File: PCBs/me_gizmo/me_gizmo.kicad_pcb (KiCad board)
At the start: 4 copper layers, 89.4 x 49.5 mm, 136 parts, among them J1 PushButton_Terminal_01x06, J2 PushButton_Terminal_01x06, J3 PushButton_Terminal_01x06, J4 PushButton_Terminal_01x06, J5 Debug, J6 USB4105-GF-A, Q1 MMBT3904L, U1 ADG714, U10 RP2350A, U11 MCP4922, U12 MCP4922, U13 MCP1702T-3302E_CB, U2 ADG714, U3 ADG714, U4 ADG714, U5 REF35250QDBVR, U6 TMP126-Q1, U7 ADG714, U8 TLV9151, U9 MCP3564R, X1 IQXO-791, X4 SG-8018CG_19.6608M-TJHSA3

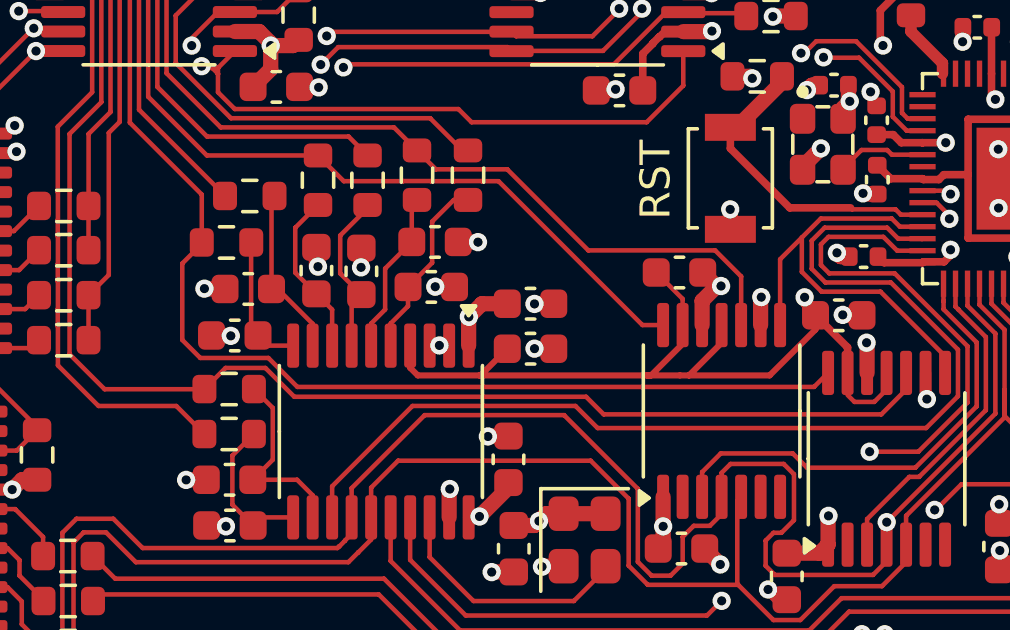
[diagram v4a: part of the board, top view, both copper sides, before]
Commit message: Switched the DAC connections on channels 3 and 4 to reflect the flipped bridge configurations
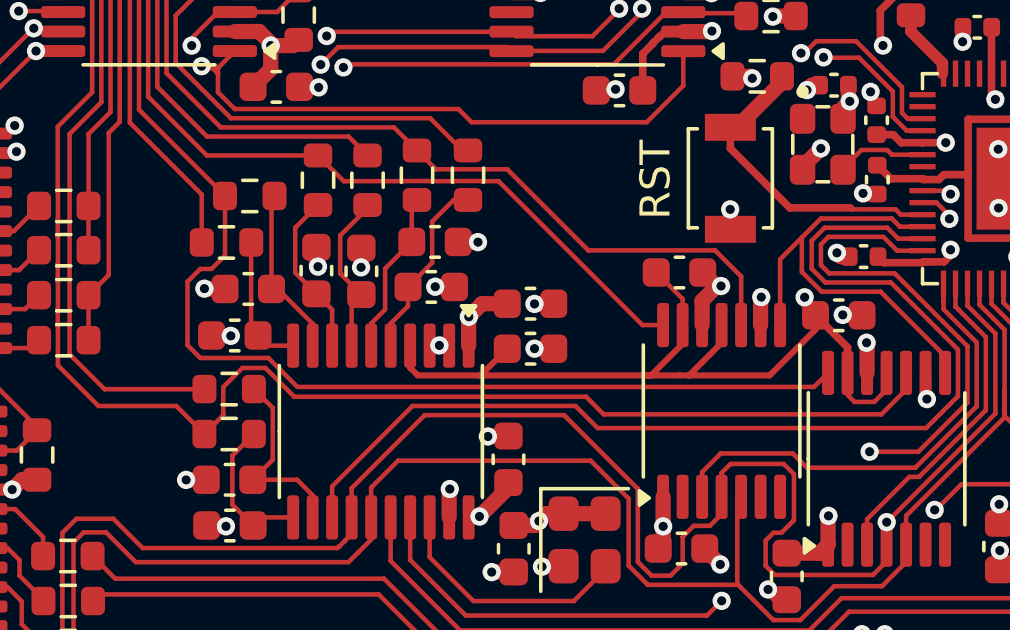
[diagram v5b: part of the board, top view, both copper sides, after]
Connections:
- U12 pad 10: /ADC/DAC/CH4/ADC4- -> /ADC/DAC/CH4/ADC4+
- U12 pad 14: /ADC/DAC/CH3/ADC3- -> /ADC/DAC/CH3/ADC3+
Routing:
- net /ADC/DAC/CH3/ADC3+: track 27.2 -> 55.0 mm
- net /ADC/DAC/CH4/ADC4+: track 48.9 -> 75.3 mm
- net /ADC/DAC/CH3/ADC3-: track 56.2 -> 30.3 mm
- net /ADC/DAC/CH4/ADC4-: track 68.8 -> 43.6 mm
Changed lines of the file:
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@@
 			(layers "F.Cu" "F.Mask" "F.Paste")
 			(roundrect_rratio 0.25)
-			(net 33 "/ADC/DAC/CH4/ADC4-")
+			(net 31 "/ADC/DAC/CH4/ADC4+")
 			(pinfunction "VOUTB")
 			(pintype "output")
@@
 			(layers "F.Cu" "F.Mask" "F.Paste")
 			(roundrect_rratio 0.25)
-			(net 26 "/ADC/DAC/CH3/ADC3-")
+			(net 28 "/ADC/DAC/CH3/ADC3+")
 			(pinfunction "VOUTA")
 			(pintype "output")
@@
 	)
 	(segment
-		(start 198.9598 94.1832)
-		(end 199.427 93.716)
-		(width 0.1524)
-		(layer "F.Cu")
-		(net 26)
-	)
-	(segment
-		(start 181.736954 94.1832)
-		(end 198.9598 94.1832)
-		(width 0.1524)
-		(layer "F.Cu")
-		(net 26)
-	)
-	(segment
-		(start 177.9004 90.067)
-		(end 177.9004 92.617336)
-		(width 0.1524)
-		(layer "F.Cu")
-		(net 26)
-	)
-	(segment
-		(start 180.771354 93.2176)
-		(end 181.736954 94.1832)
-		(width 0.1524)
-		(layer "F.Cu")
-		(net 26)
-	)
-	(segment
 		(start 176.4284 78.486)
 		(end 176.4284 79.026198)
@@
 	)
 	(segment
-		(start 178.5498 89.4176)
-		(end 177.9004 90.067)
-		(width 0.1524)
-		(layer "F.Cu")
-		(net 26)
-	)
-	(segment
 		(start 174.784049 77.7864)
 		(end 174.859655 77.710794)
@@
 	)
 	(segment
-		(start 177.9004 92.617336)
-		(end 178.500664 93.2176)
-		(width 0.1524)
-		(layer "F.Cu")
-		(net 26)
-	)
-	(segment
 		(start 173.9292 77.7864)
 		(end 174.784049 77.7864)
@@
 	)
 	(segment
-		(start 178.500664 93.2176)
-		(end 180.771354 93.2176)
-		(width 0.1524)
-		(layer "F.Cu")
-		(net 26)
-	)
-	(segment
 		(start 176.151965 79.302633)
 		(end 176.151965 85.372365)
@@
 	)
 	(segment
+		(start 180.771354 93.2176)
+		(end 178.500664 93.2176)
+		(width 0.1524)
+		(layer "F.Cu")
+		(net 28)
+	)
+	(segment
+		(start 181.736954 94.1832)
+		(end 180.771354 93.2176)
+		(width 0.1524)
+		(layer "F.Cu")
+		(net 28)
+	)
+	(segment
 		(start 179.3248 87.8086)
 		(end 176.457766 84.941566)
@@
 	)
 	(segment
+		(start 179.3248 89.8002)
+		(end 179.3248 87.8176)
+		(width 0.1524)
+		(layer "F.Cu")
+		(net 28)
+	)
+	(segment
+		(start 178.075 90.675)
+		(end 178.5 90.25)
+		(width 0.1524)
+		(layer "F.Cu")
+		(net 28)
+	)
+	(segment
 		(start 174.8963 76.075696)
 		(end 174.8963 70.7817)
@@
 	)
 	(segment
+		(start 178.075 92.791936)
+		(end 178.075 90.675)
+		(width 0.1524)
+		(layer "F.Cu")
+		(net 28)
+	)
+	(segment
+		(start 198.9598 94.1832)
+		(end 181.736954 94.1832)
+		(width 0.1524)
+		(layer "F.Cu")
+		(net 28)
+	)
+	(segment
+		(start 199.427 93.716)
+		(end 198.9598 94.1832)
+		(width 0.1524)
+		(layer "F.Cu")
+		(net 28)
+	)
+	(segment
+		(start 178.5 90.25)
+		(end 178.875 90.25)
+		(width 0.1524)
+		(layer "F.Cu")
+		(net 28)
+	)
+	(segment
 		(start 174.8963 70.7817)
 		(end 174.0916 69.977)
@@
 	)
 	(segment
+		(start 178.500664 93.2176)
+		(end 178.075 92.791936)
+		(width 0.1524)
+		(layer "F.Cu")
+		(net 28)
+	)
+	(segment
+		(start 178.875 90.25)
+		(end 179.3248 89.8002)
+		(width 0.1524)
+		(layer "F.Cu")
+		(net 28)
+	)
+	(segment
 		(start 174.09 69.95)
 		(end 174.09 64.95)
@@
 	)
 	(segment
+		(start 201.201796 95.0976)
+		(end 191.9478 95.0976)
+		(width 0.1524)
+		(layer "F.Cu")
+		(net 31)
+	)
+	(segment
 		(start 173.75 88.613088)
 		(end 173.75 89.161912)
@@
 	)
 	(segment
+		(start 179.2676 94.187112)
+		(end 179.2676 95.1228)
+		(width 0.1524)
+		(layer "F.Cu")
+		(net 31)
+	)
+	(segment
 		(start 173.9292 80.3864)
 		(end 174.4864 80.3864)
@@
 	)
 	(segment
+		(start 179.2676 95.1228)
+		(end 178.637 95.7534)
+		(width 0.1524)
+		(layer "F.Cu")
+		(net 31)
+	)
+	(segment
 		(start 174.8963 84.3615)
 		(end 173.75 85.5078)
@@
 	)
 	(segment
+		(start 202.027 94.272396)
+		(end 201.201796 95.0976)
+		(width 0.1524)
+		(layer "F.Cu")
+		(net 31)
+	)
+	(segment
 		(start 173.7546 89.166512)
 		(end 173.7546 90.083488)
@@
 	)
 	(segment
+		(start 202.027 93.716)
+		(end 202.027 94.272396)
+		(width 0.1524)
+		(layer "F.Cu")
+		(net 31)
+	)
+	(segment
 		(start 173.7546 88.608488)
 		(end 173.75 88.613088)
@@
 	)
 	(segment
+		(start 191.9478 95.0976)
+		(end 191.3616 94.5114)
+		(width 0.1524)
+		(layer "F.Cu")
+		(net 31)
+	)
+	(segment
 		(start 173.75 87.686912)
 		(end 173.7546 87.691512)
@@
 	)
 	(segment
+		(start 180.671488 93.5502)
+		(end 179.904512 93.5502)
+		(width 0.1524)
+		(layer "F.Cu")
+		(net 31)
+	)
+	(segment
 		(start 173.7546 92.166512)
 		(end 173.7546 93.4652)
@@
 	)
 	(segment
+		(start 179.904512 93.5502)
+		(end 179.2676 94.187112)
+		(width 0.1524)
+		(layer "F.Cu")
+		(net 31)
+	)
+	(segment
+		(start 181.632688 94.5114)
+		(end 180.671488 93.5502)
+		(width 0.1524)
+		(layer "F.Cu")
+		(net 31)
+	)
+	(segment
 		(start 177.7018 94.8182)
 		(end 178.637 95.7534)
@@
 		(net 31)
 	)
+	(segment
+		(start 191.3616 94.5114)
+		(end 181.632688 94.5114)
+		(width 0.1524)
+		(layer "F.Cu")
+		(net 31)
+	)
 	(via
 		(at 159.131 74.0918)
@@
 	)
 	(segment
-		(start 201.201796 95.0976)
-		(end 191.9478 95.0976)
-		(width 0.1524)
-		(layer "F.Cu")
-		(net 33)
-	)
-	(segment
 		(start 175.2021 79.802904)
 		(end 174.485596 79.0864)
@@
 	)
 	(segment
-		(start 180.671488 93.5502)
-		(end 179.3426 93.5502)
-		(width 0.1524)
-		(layer "F.Cu")
-		(net 33)
-	)
-	(segment
 		(start 173.372804 79.0864)
 		(end 173.126404 78.84)
@@
 	)
 	(segment
-		(start 202.027 94.272396)
-		(end 201.201796 95.0976)
-		(width 0.1524)
-		(layer "F.Cu")
-		(net 33)
-	)
-	(segment
 		(start 173.049804 78.7634)
 		(end 170.3705 78.7634)
@@
 	)
 	(segment
-		(start 202.027 93.716)
-		(end 202.027 94.272396)
-		(width 0.1524)
-		(layer "F.Cu")
-		(net 33)
-	)
-	(segment
 		(start 175.3108 94.2594)
 		(end 174.1424 93.091)
@@
 	)
 	(segment
-		(start 179.3426 93.5502)
-		(end 178.638 94.2548)
-		(width 0.1524)
-		(layer "F.Cu")
-		(net 33)
-	)
-	(segment
 		(start 173.9292 79.0864)
 		(end 173.372804 79.0864)
@@
 	)
 	(segment
-		(start 191.9478 95.0976)
-		(end 191.3616 94.5114)
-		(width 0.1524)
-		(layer "F.Cu")
-		(net 33)
-	)
-	(segment
 		(start 174.1424 93.091)
 		(end 174.1424 85.7504)
@@
 	)
 	(segment
-		(start 181.632688 94.5114)
-		(end 180.671488 93.5502)
-		(width 0.1524)
-		(layer "F.Cu")
-		(net 33)
-	)
-	(segment
 		(start 178.6334 94.2594)
 		(end 175.3108 94.2594)
 		(width 0.1524)
 		(layer "F.Cu")
-		(net 33)
-	)
-	(segment
-		(start 191.3616 94.5114)
-		(end 181.632688 94.5114)
-		(width 0.1524)
-		(layer "F.Cu")

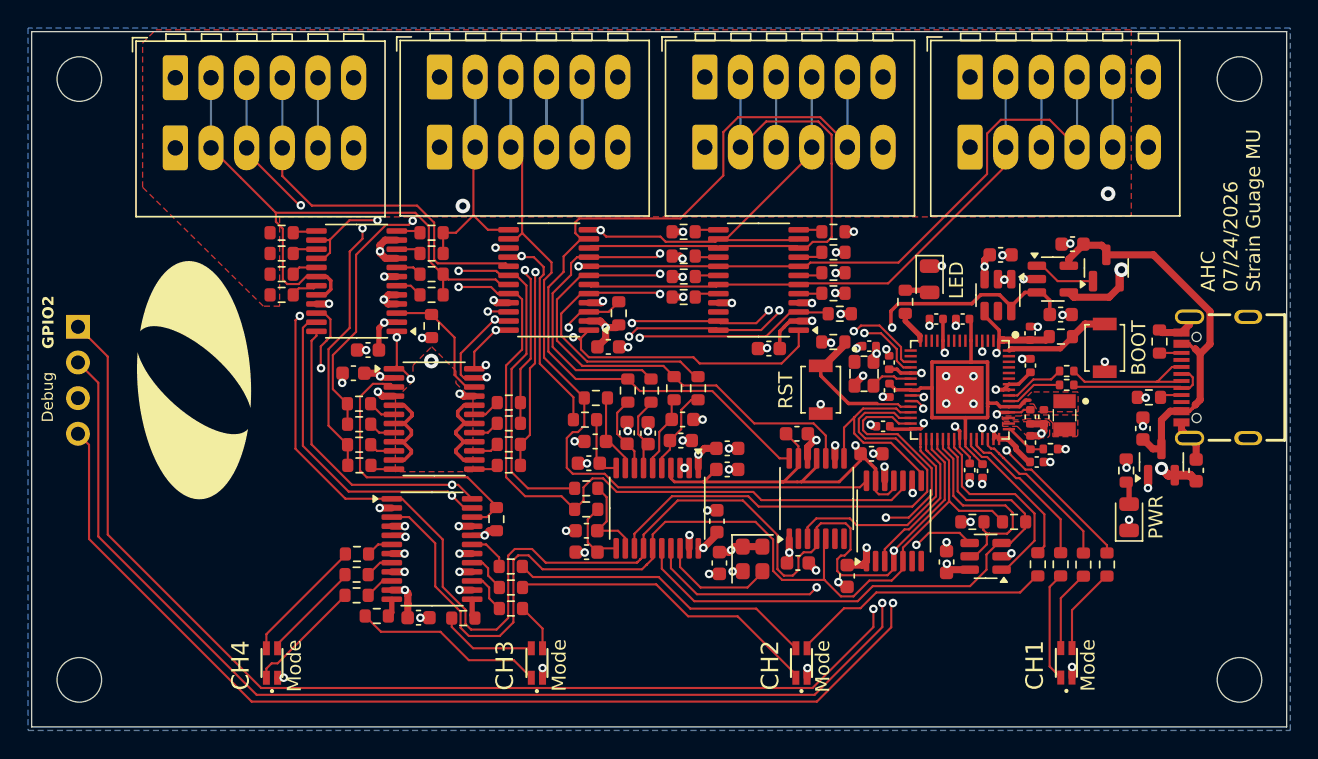
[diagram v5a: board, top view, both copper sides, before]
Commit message: Added Main.py with a channel configuration detection script. Also added a thread that updates the leds to display what the device thinks the current operating mode is, particularly while actively looping detect_config. Finally, there are a bunch of untested updates (mostly software) to make the code compatible with the new board. Any replaced working protoype code exists underneath the revisions labeled with 'protptype above it. This commit contains a few key revisions to the hardware including pulling all of the RGB LEDs to ground so that they can be enabled, and pull down resistors on the adc channels that are not connected to the DAC.
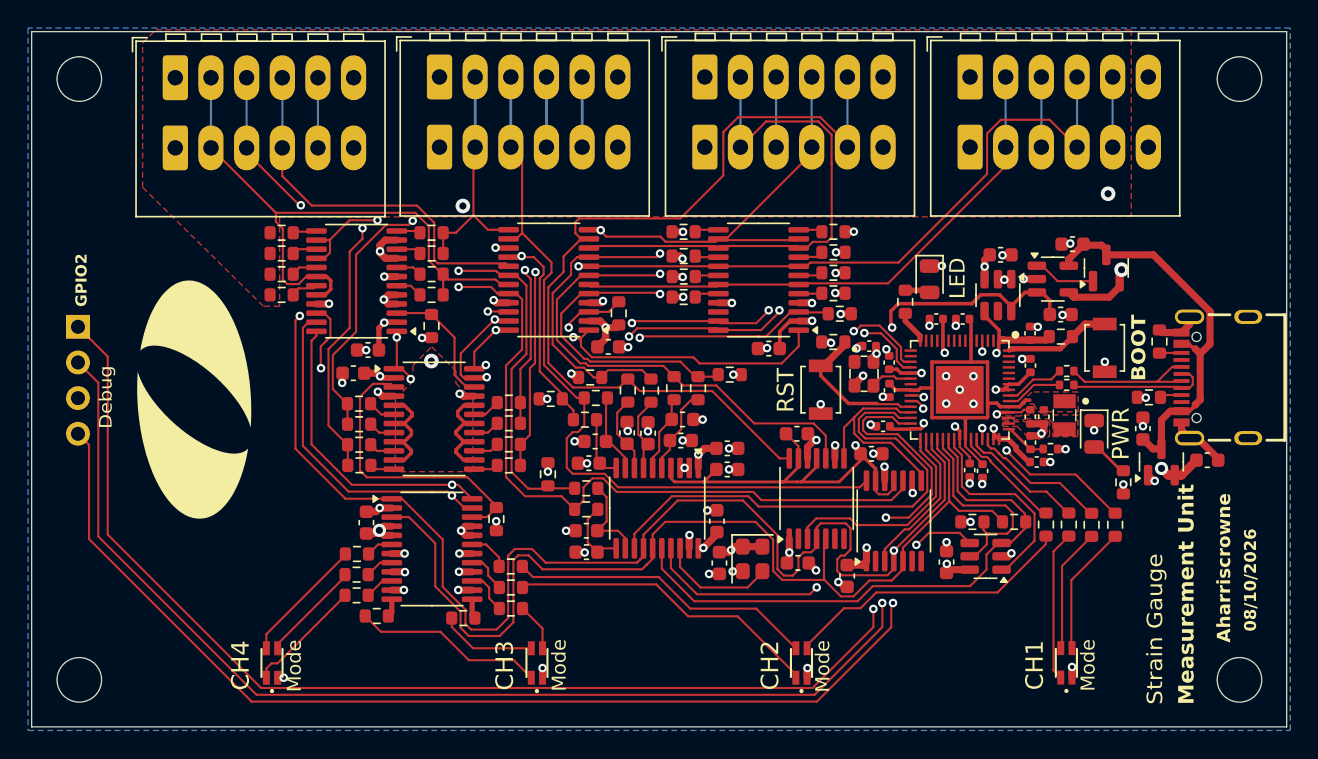
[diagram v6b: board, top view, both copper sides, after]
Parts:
- added R60: 100kΩ, Resistor_SMD:R_0603_1608Metric, F.Cu at (176.7, 93.3)
- added R61: 100kΩ, Resistor_SMD:R_0603_1608Metric, F.Cu at (176.9, 87.9)
- added R62: 100kΩ, Resistor_SMD:R_0603_1608Metric, F.Cu at (189.7, 86.2)
- added R63: 100kΩ, Resistor_SMD:R_0603_1608Metric, F.Cu at (179.7, 86.4)
- moved C20 7.72 mm to (163.8, 96.7), turned to -90 degrees
- moved D3 6.44 mm to (215.6, 90.4), turned to -90 degrees
- moved R50 2.89 mm to (213.8, 96.8)
- moved R51 2.89 mm to (215.5, 96.9)
- moved R52 2.89 mm to (217.1, 96.9)
- moved R55 2.89 mm to (212.2, 96.8)
- moved svg2mod 1.38 mm to (151.5, 87.9)
- moved C3 1.08 mm to (223.7, 92.3), turned to 0 degrees
- moved R47 0.86 mm to (217.7, 93.8), turned to 90 degrees
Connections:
- U7 pad 11: +3V3 -> GND
- U7 pad 14: +3V3 -> GND
- U7 pad 16: +3V3 -> GND
- U7 pad 18: +3V3 -> GND
- U7 pad 20: +3V3 -> GND
- U7 pad 5: +3V3 -> GND
- U7 pad 7: +3V3 -> GND
- U7 pad 9: +3V3 -> GND
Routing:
- net GND: track 67.0 -> 78.0 mm, vias 77 -> 86
- net +3V3: track 82.7 -> 74.3 mm, vias 42 -> 35
- net Net-(D4-Pad2): track 5.82 -> 8.86 mm
- net Net-(D4-Pad1): track 7.90 -> 10.7 mm
- net /GPIO26: track 10.7 -> 7.87 mm
- net Net-(D4-Pad4): track 6.48 -> 9.28 mm
- net Net-(D5-Pad4): track 18.7 -> 20.8 mm
- net /GPIO27: track 11.0 -> 9.03 mm
- net Net-(D3-A): track 1.65 -> 3.24 mm
- net /GPIO29: track 11.4 -> 9.85 mm
- net /ADC/DAC/CH1/ADC1+: track 57.7 -> 59.2 mm
- net /ADC/DAC/CH2/ADC2-: track 61.5 -> 62.5 mm
- net /GPIO28: track 14.2 -> 13.3 mm
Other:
- board text added: "08/10/2026"
- board text added: "Aharriscrowne"
- board text added: "Measurement Unit"
- board text added: "Strain Gauge"
- board text removed: "AHC 07/24/2026 Strain Guage MU"
